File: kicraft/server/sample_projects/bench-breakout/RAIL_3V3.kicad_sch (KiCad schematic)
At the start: 3 parts, among them U2 AMS1117-3.3

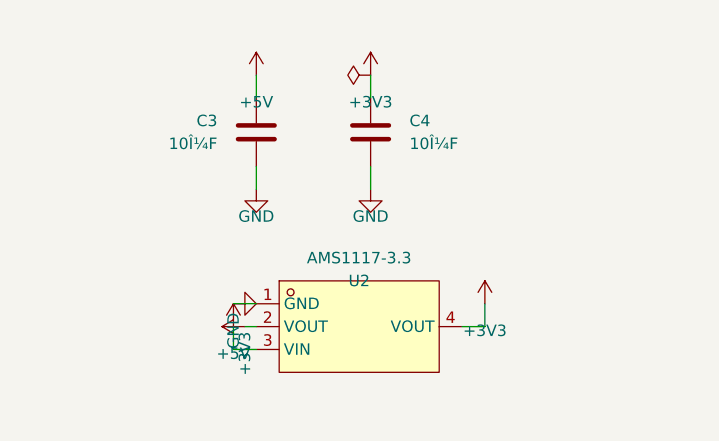
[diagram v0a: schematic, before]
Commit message: feat(showcase): refresh landing samples from self-eval 20260614
Promote the three best boards from self-eval batch 20260614T215540Z
(all grade B) into the landing-page showcase, replacing the regressed
PIR night light (D/45, hit erc_errors + unprogrammable_mcu gates):

- usb-pd-trigger (NEW, featured hero) — 81.0, fab-ready
- weather-sensor (re-promoted; stem A_BMP280_BAROMETRIC -> BMP280_QWIIC_USB_C)
- bench-breakout (re-promoted; 4->5 sheets, 16->19 parts)

Regenerated board.png/hero.png renders and interactive board.glb models
via scripts/promote_to_sample.py. Already live (deploy/restart-web.sh).

Co-Authored-By: Claude Opus 4.8 (1M context) <noreply@anthropic.com>
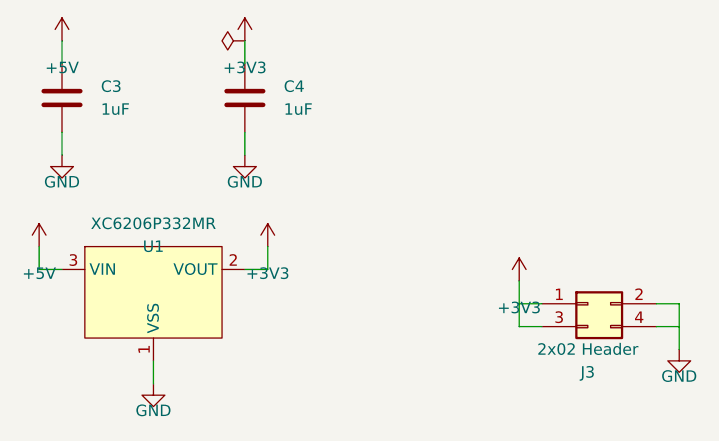
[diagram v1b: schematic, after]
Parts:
- removed U2: AMS1117-3.3, ams1117-3v3:SOT-223-3_L6.5-W3.4-P2.30-LS7.0-BR, symbol ams1117-3v3:AMS1117-3.3
- added J3: 2x02 Header, Connector_PinHeader_2.54mm:PinHeader_2x02_P2.54mm_Vertical, symbol Connector_Generic:Conn_02x02_Odd_Even
- added U1: XC6206P332MR, xc6206p332mr:SOT-23-3_L2.9-W1.3-P1.90-LS2.4-BR, symbol xc6206p332mr:XC6206P332MR_C5148692
- C3, C4: value 10Î¼F -> 1uF
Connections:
- net +3V3: now also J3.1 (Pin_1), J3.3 (Pin_3), U1.2 (VOUT)
- net +5V: now also U1.3 (VIN)
- net GND: now also J3.2 (Pin_2), J3.4 (Pin_4), U1.1 (VSS)
